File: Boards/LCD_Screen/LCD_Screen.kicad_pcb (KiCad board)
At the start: 2 copper layers, 172.4 x 111.9 mm, 33 parts, among them J1 MicroFit_VT_4, U1 MCP25625-x-SS, U2 Raspberry_Pi_Zero, U3 TPS563231, Y1 Crystal_SMD

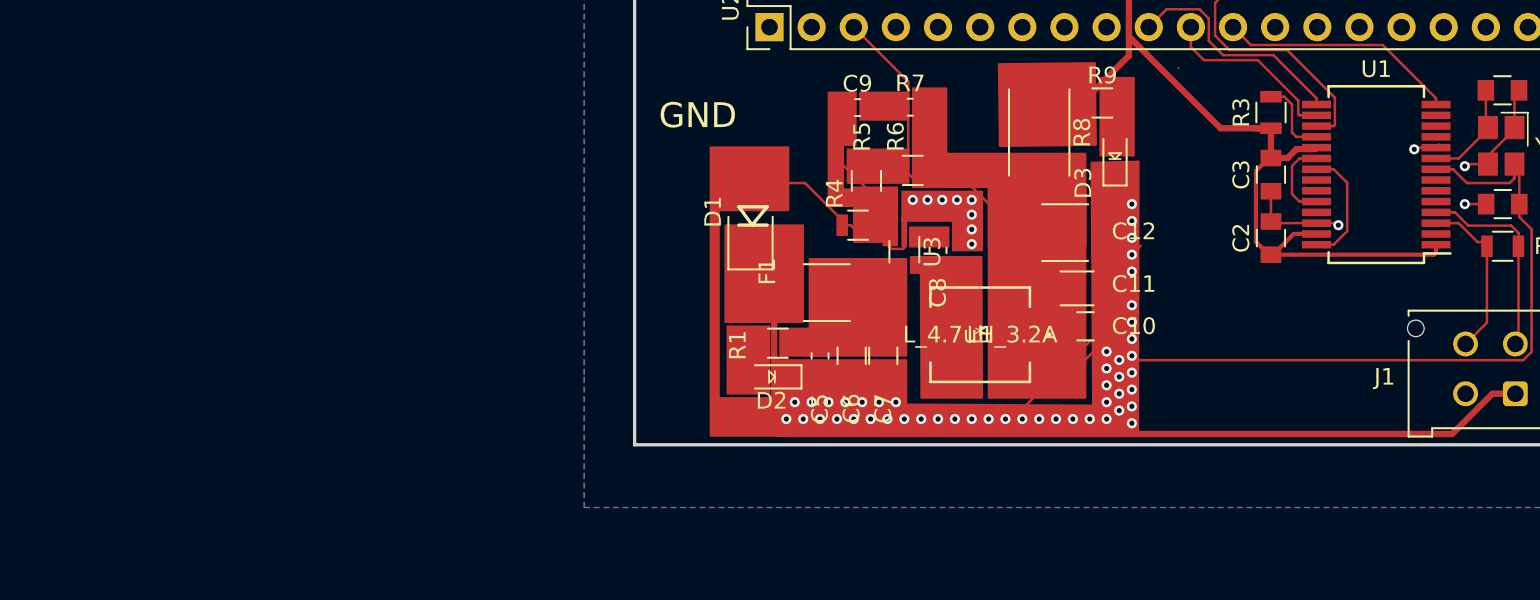
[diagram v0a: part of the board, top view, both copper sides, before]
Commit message: Fixed Buck for LCD Screen
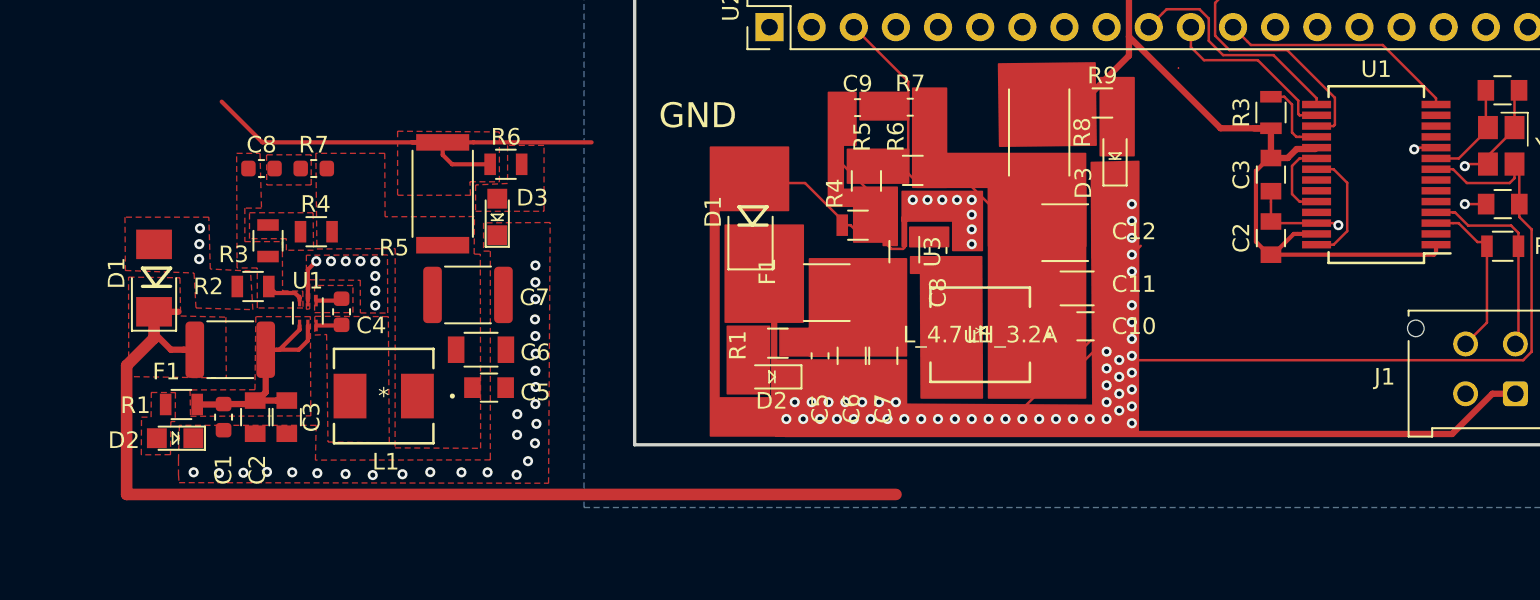
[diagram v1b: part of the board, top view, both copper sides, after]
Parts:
- added C1: C_0.1uF, footprints:C_0603_1608Metric, F.Cu at (181.0, 51.2)
- added C2: C_10uF_25V, footprints:C_0805_OEM, F.Cu at (182.9, 51.2)
- added C3: C_10uF_25V, footprints:C_0805_OEM, F.Cu at (184.8, 51.2)
- added C4: C_0.1uF_0603, footprints:C_0603_1608Metric, F.Cu at (188.1, 44.8)
- added C5: C_10uF, footprints:C_0805_OEM, F.Cu at (197.0, 49.4)
- added C6: C_22uF, footprints:C_1206_OEM, F.Cu at (196.5, 47.1)
- added C7: C_33uF, Capacitor_SMD:C_1812_4532Metric, F.Cu at (195.7, 43.8)
- added C8: C_100nF, footprints:C_0603_1608Metric, F.Cu at (183.2, 36.2)
- added D1: D_Zener_18V, footprints:DO-214AA, F.Cu at (176.8, 42.8)
- added D2: LED_0805, footprints:LED_0805_OEM, F.Cu at (178.0, 52.5)
- added D3: LED_0805, footprints:LED_0805_OEM, F.Cu at (197.5, 39.1)
- added F1: F_2.6A_16V, Fuse:Fuse_1812_4532Metric, F.Cu at (181.4, 47.1)
- added L1: L_4.7uH_3.2A, footprints:IHLP2020BZER4R7M11, F.Cu at (190.6, 49.9)
- added R1: R_1K, footprints:R_0805_OEM, F.Cu at (178.4, 50.4)
- added R2: R_10K, footprints:R_0805_OEM, F.Cu at (182.7, 43.3)
- added R3: R_51.1K, footprints:R_0805_OEM, F.Cu at (183.6, 40.6)
- added R4: R_22K, footprints:R_0805_OEM, F.Cu at (186.6, 40.0)
- added R5: R_0_2512, footprints:R_2512_OEM, F.Cu at (194.2, 37.7)
- added R6: R_200, footprints:R_0805_OEM, F.Cu at (198.0, 36.0)
- added R7: R_1, footprints:R_0603_1608Metric, F.Cu at (186.4, 36.2)
- added U1: TPS563231, footprints:SOT-563, F.Cu at (186.0, 44.9)
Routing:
- net (no net): track 0.00 -> 116.6 mm, vias 0 -> 38
- added copper zone on F.Cu, net (none)

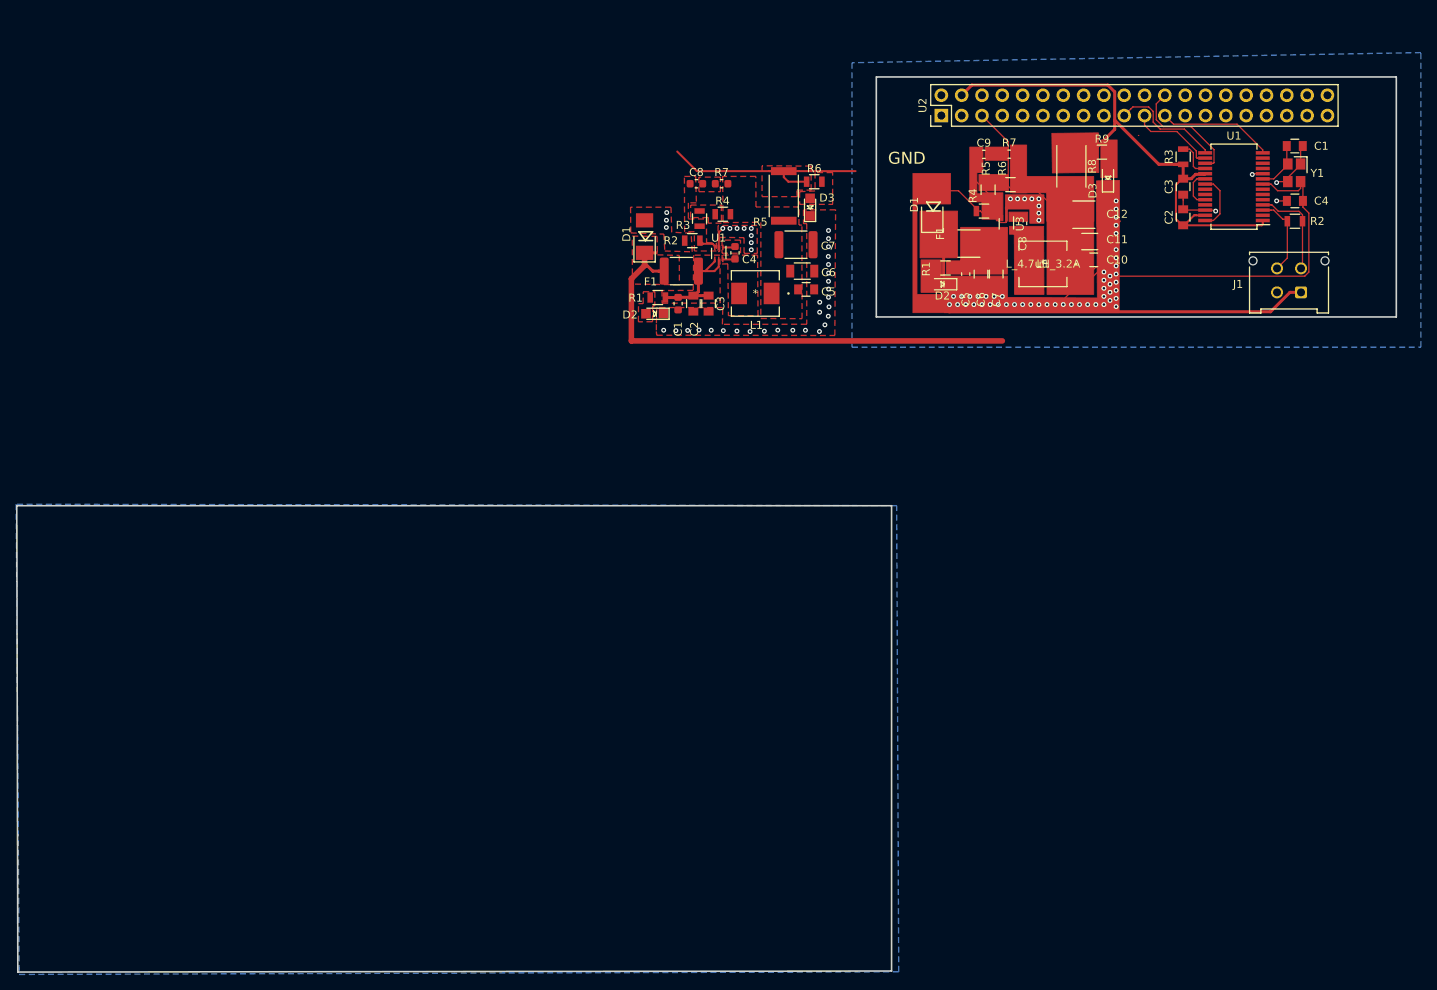
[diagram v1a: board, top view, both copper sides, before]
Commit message: Fixing errors in LCD buck
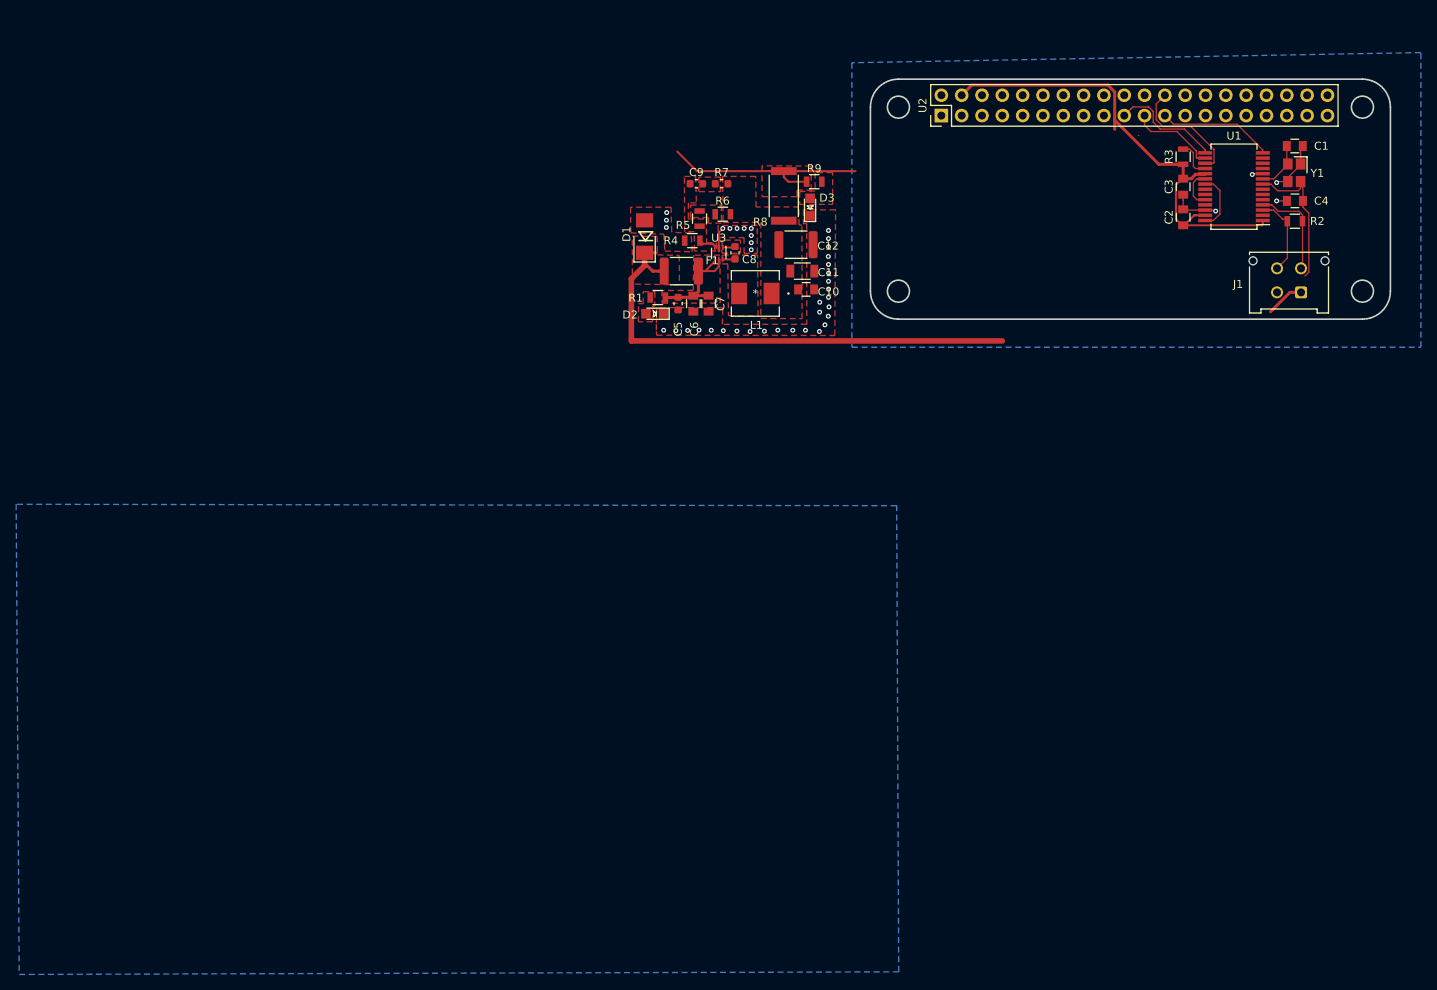
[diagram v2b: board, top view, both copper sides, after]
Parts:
- removed the C10 at (232.9, 45.7)
- removed the C11 at (232.4, 43.4)
- removed the C12 at (231.7, 40.1)
- removed the C5 at (216.9, 47.5)
- removed the C6 at (218.8, 47.5)
- removed the C7 at (220.7, 47.5)
- removed the C8 at (183.2, 36.2)
- removed the C8 at (224.0, 41.1)
- removed the D1 at (212.7, 39.1)
- removed the D2 at (214.0, 48.8)
- removed the D3 at (234.7, 35.4)
- removed the F1 at (217.3, 43.7)
- removed the L1 at (226.6, 46.2)
- removed the R1 at (214.4, 46.7)
- removed the R4 at (219.2, 39.6)
- removed the R5 at (219.7, 37.0)
- removed the R6 at (222.5, 36.3)
- removed the R7 at (222.4, 32.5)
- removed the R8 at (230.1, 34.0)
- removed the R9 at (233.9, 32.3)
- removed the U3 at (222.0, 41.2)
- C12: renamed from C7; footprint Capacitor_SMD:C_1812_4532Metric -> footprints:C_1812_4532Metric
- F1: footprint Fuse:Fuse_1812_4532Metric -> footprints:Fuse_1812_4532Metric
- R2: value R_100 -> R_120_DNP
- moved C9 36.1 mm to (183.2, 36.2)
- turned F1 to 0 degrees
- renumbered C5 to C10, C6 to C11, C1 to C5, C2 to C6, C3 to C7, C4 to C8, R2 to R4, R3 to R5, R4 to R6, R5 to R8, R6 to R9, U1 to U3
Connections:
- C10 pad 1: (no net) -> Net-(C10-Pad1)
- C10 pad 2: (no net) -> GND
- C11 pad 1: (no net) -> Net-(C10-Pad1)
- C11 pad 2: (no net) -> GND
- C12 pad 1: (no net) -> Net-(C10-Pad1)
- C12 pad 2: (no net) -> GND
- C5 pad 1: (no net) -> Net-(C5-Pad1)
- C5 pad 2: (no net) -> GND
- C6 pad 1: (no net) -> Net-(C5-Pad1)
- C6 pad 2: (no net) -> GND
- C7 pad 1: (no net) -> Net-(C5-Pad1)
- C7 pad 2: (no net) -> GND
- C8 pad 1: (no net) -> Net-(C8-Pad1)
- C8 pad 2: (no net) -> Net-(C8-Pad2)
- D1 pad 1: (no net) -> /12V
- D1 pad 2: (no net) -> GND
- D2 pad 1: (no net) -> GND
- D2 pad 2: (no net) -> Net-(D2-Pad2)
- D3 pad 1: (no net) -> GND
- D3 pad 2: (no net) -> Net-(D3-Pad2)
- F1 pad 1: (no net) -> /12V
- F1 pad 2: (no net) -> Net-(C5-Pad1)
- L1 pad 1: (no net) -> Net-(C10-Pad1)
- L1 pad 2: (no net) -> Net-(C8-Pad1)
- R1 pad 1: (no net) -> Net-(C5-Pad1)
- R1 pad 2: (no net) -> Net-(D2-Pad2)
- R4 pad 1: (no net) -> Net-(C9-Pad1)
- R4 pad 2: (no net) -> GND
- R5 pad 1: (no net) -> Net-(R5-Pad1)
- R5 pad 2: (no net) -> Net-(C9-Pad1)
- R6 pad 1: (no net) -> Net-(C10-Pad1)
- R6 pad 2: (no net) -> Net-(R5-Pad1)
- R7 pad 1: (no net) -> Net-(C9-Pad2)
- R7 pad 2: (no net) -> Net-(C10-Pad1)
- R8 pad 1: (no net) -> VCC
- R8 pad 2: (no net) -> Net-(C10-Pad1)
- R9 pad 1: (no net) -> VCC
- R9 pad 2: (no net) -> Net-(D3-Pad2)
- U3 pad 1: (no net) -> Net-(C8-Pad2)
- U3 pad 2: (no net) -> GND
- U3 pad 3: (no net) -> Net-(C9-Pad1)
- U3 pad 4: (no net) -> Net-(C5-Pad1)
- U3 pad 5: (no net) -> Net-(C5-Pad1)
- U3 pad 6: (no net) -> Net-(C8-Pad1)
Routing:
- net (no net): track 116.6 -> 0.25 mm, vias 38 -> 0
- net Net-(U2-Pad5): track 60.0 -> 0.00 mm
- net GND: track 56.4 -> 17.7 mm, vias 60 -> 42
- net Net-(C10-Pad1): track 25.4 -> 0.00 mm
- net Net-(C4-Pad1): track 42.0 -> 18.7 mm
- net VCC: track 72.6 -> 90.9 mm
- net /12V: track 57.9 -> 68.3 mm
- net Net-(C9-Pad1): track 11.0 -> 2.31 mm
- net Net-(C8-Pad1): track 6.10 -> 1.60 mm
- net Net-(D2-Pad2): track 2.25 -> 0.00 mm
- net Net-(D3-Pad2): track 2.15 -> 0.00 mm
- net Net-(R5-Pad1): track 1.97 -> 0.00 mm
- net Net-(C9-Pad2): track 1.61 -> 0.00 mm
- net Net-(C5-Pad1): track 14.4 -> 15.2 mm
- added copper zone on F.Cu, net /12V
- added copper zone on F.Cu, net Net-(C10-Pad1)
- added copper zone on F.Cu, net Net-(C5-Pad1)
- added copper zone on F.Cu, net Net-(C8-Pad1)
- added copper zone on F.Cu, net Net-(C8-Pad2)
- added copper zone on F.Cu, net Net-(C9-Pad1)
- added copper zone on F.Cu, net Net-(C9-Pad2)
- added copper zone on F.Cu, net Net-(D2-Pad2)
- added copper zone on F.Cu, net Net-(D3-Pad2)
- added copper zone on F.Cu, net Net-(R5-Pad1)
- added copper zone on F.Cu, net VCC
- removed copper zone on F.Cu, net (none)
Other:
- board size 172.4 x 111.9 mm -> 65 x 30 mm
- board text removed: "GND"

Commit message: final lcd screen board
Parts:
- moved C1 98.0 mm to (177.0, 86.6)
- moved C4 98.0 mm to (177.0, 93.5)
- moved J1 98.0 mm to (177.8, 104.9)
- moved R2 98.0 mm to (177.0, 96.0)
- moved Y1 98.0 mm to (176.9, 90.0)
- moved C2 98.0 mm to (163.1, 95.5)
- moved C3 98.0 mm to (163.1, 91.7)
- moved R3 98.0 mm to (163.1, 88.0)
- moved U1 98.0 mm to (169.4, 91.7)
- moved U2 98.0 mm to (132.8, 82.8)
- moved C10 68.0 mm to (152.0, 100.5)
- moved C11 68.0 mm to (151.5, 98.2)
- moved C12 68.0 mm to (150.7, 94.9)
- moved C5 68.0 mm to (136.0, 102.2)
- moved C6 68.0 mm to (137.9, 102.2)
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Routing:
- net VCC: track 90.9 -> 71.3 mm
- net Net-(C4-Pad1): track 18.7 -> 8.74 mm
- net /12V: track 68.3 -> 60.0 mm

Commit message: final final lcd board - added silk screen.
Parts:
- removed the G*** at (126.7, 103.6)
- moved L1 94.8 mm to (219.3, 41.3)
- moved C1 94.8 mm to (250.7, 26.9)
- moved C10 94.8 mm to (225.7, 40.8)
- moved C11 94.8 mm to (225.2, 38.5)
- moved C3 94.8 mm to (236.7, 32.0)
- moved C9 94.8 mm to (212.0, 27.6)
- moved D1 94.8 mm to (205.5, 34.2)
- moved D2 94.8 mm to (206.7, 43.8)
- moved F1 94.8 mm to (210.1, 38.5)
- moved R6 94.8 mm to (215.3, 31.4)
- moved R7 94.8 mm to (215.1, 27.6)
- moved R8 94.8 mm to (222.9, 29.1)
- moved U1 94.8 mm to (243.1, 32.0)
- moved Y1 94.8 mm to (250.6, 30.3)
- moved C12 94.8 mm to (224.4, 35.2)
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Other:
- board text added: "1/4/2020"
- board text added: "Jackie Zeng"
- board text added: "LCD Board Rev 1"

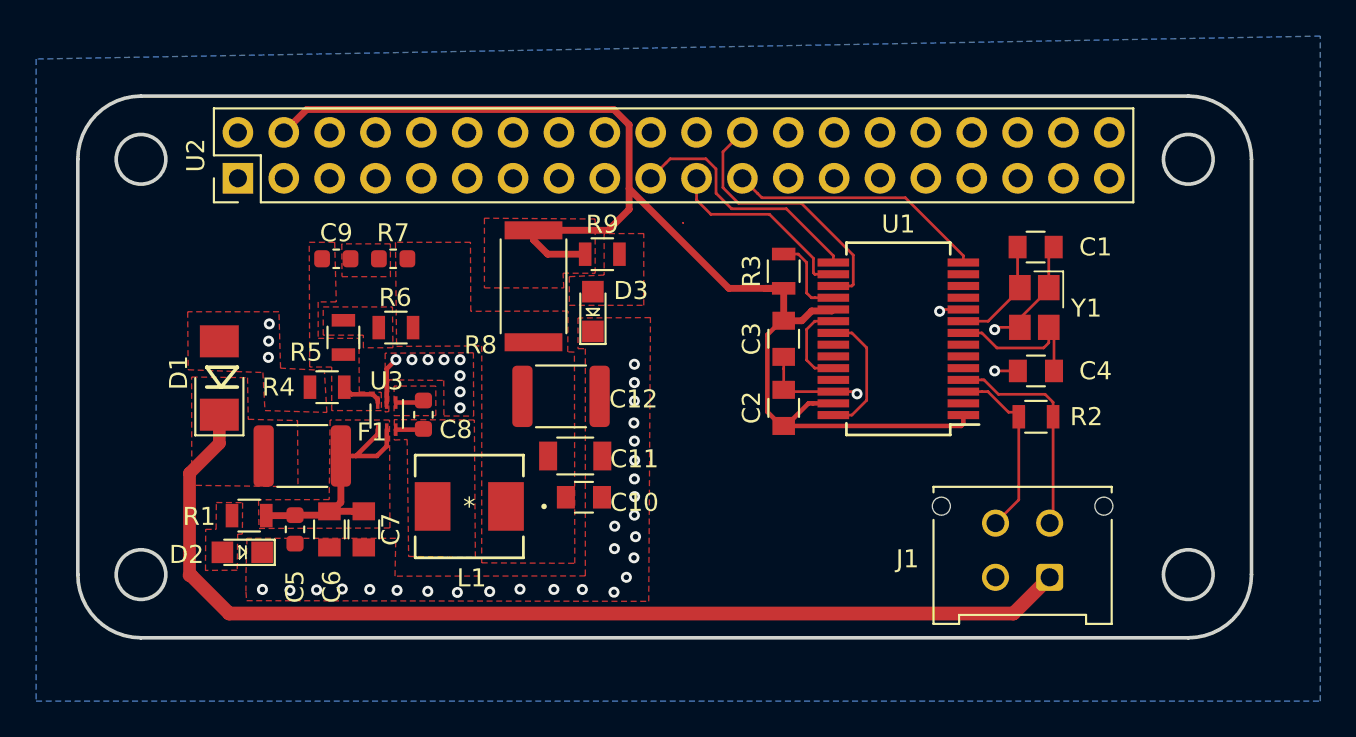
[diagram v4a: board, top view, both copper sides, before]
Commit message: fixed trace sizes, added text for LEDs, and changed board size.
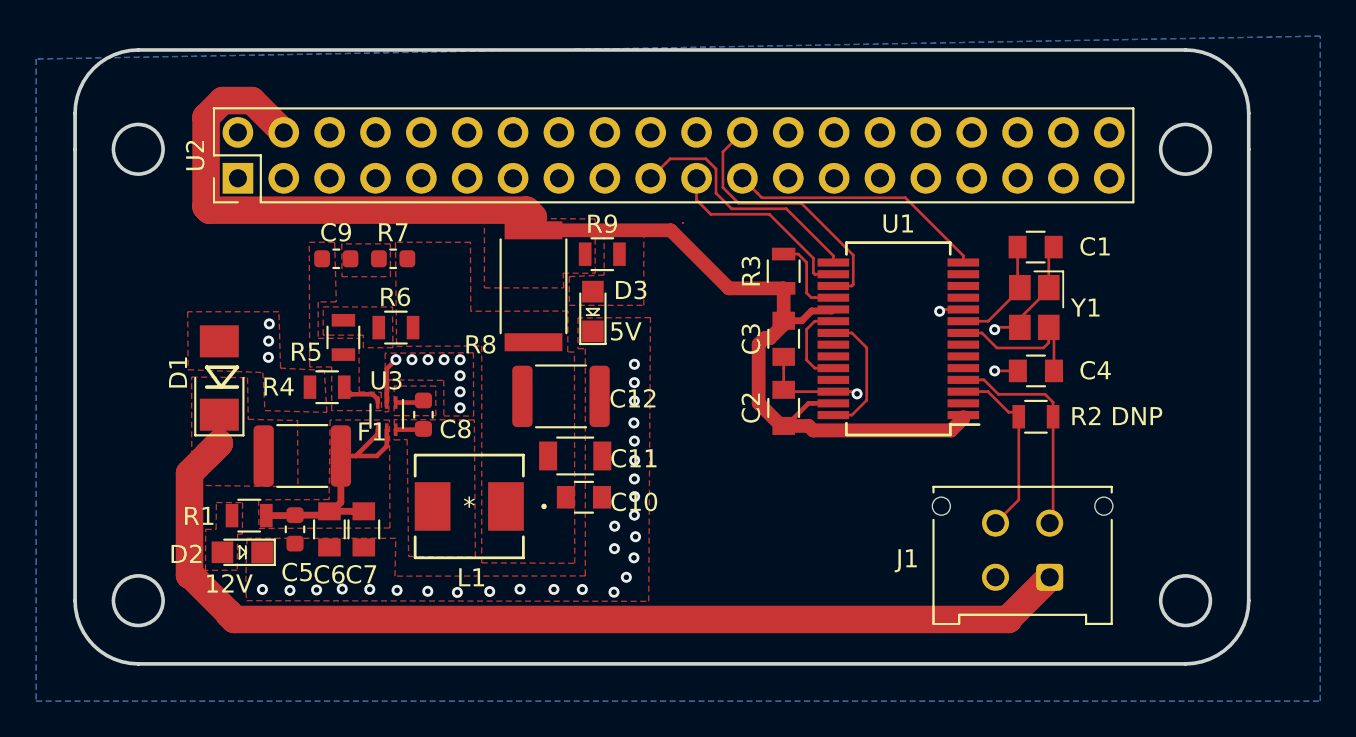
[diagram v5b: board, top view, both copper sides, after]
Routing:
- net VCC: track 71.3 -> 83.4 mm
- net /12V: track 60.0 -> 68.3 mm
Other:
- board size 65 x 30 mm -> 65 x 34 mm
- board text added: "1/11/2020"
- board text added: "12V"
- board text added: "5V"
- board text added: "DNP"
- board text added: "RaspPi goes on this side"
- board text removed: "1/4/2020"
